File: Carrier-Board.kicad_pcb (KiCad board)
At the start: 4 copper layers, 92 x 96 mm, 50 parts, among them J1 CONN_3-6318491-6, J10 Conn_02x03_Odd_Even, J2 Conn_01x0, J4 SI-51009-F, J6 Conn_01x03_Male, J7 Conn_01x03_Male, J8 Conn_01x06_Male, J9 Conn_02x04_Odd_Even, SW1 SW_Push, SW2 SW_Push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

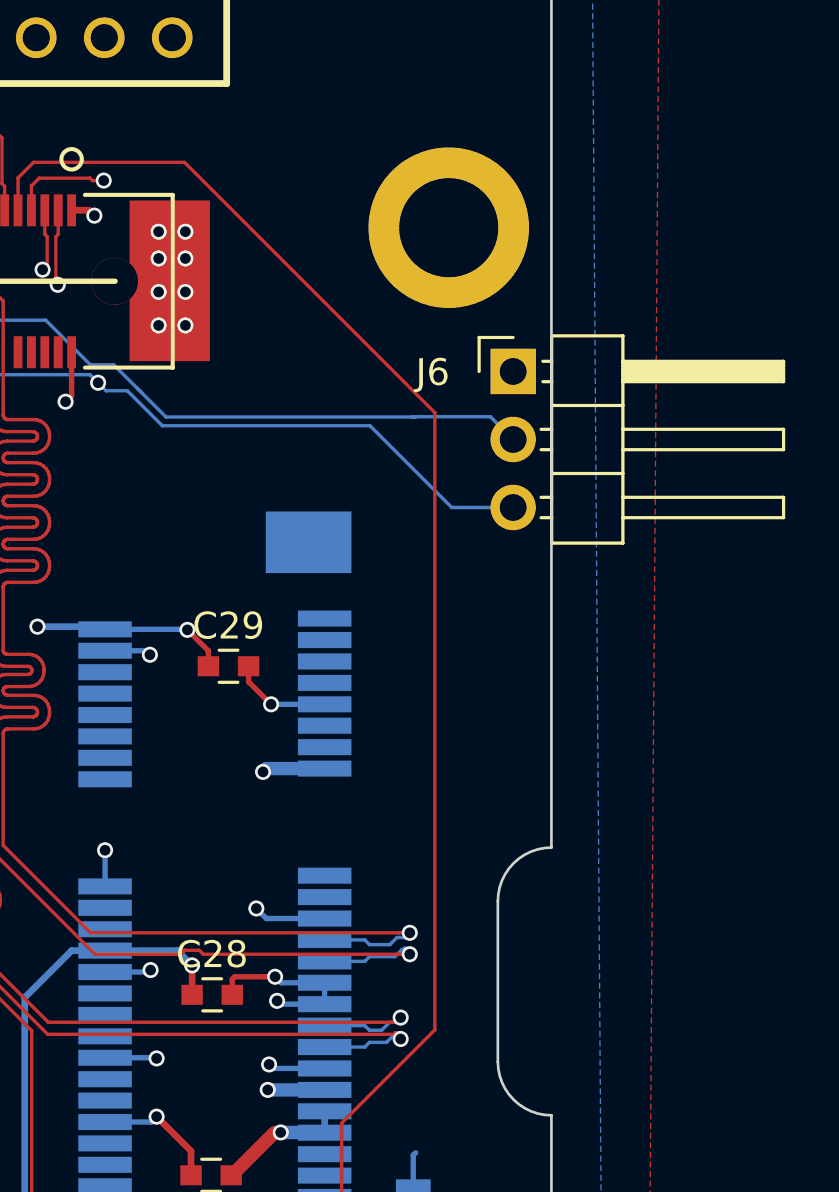
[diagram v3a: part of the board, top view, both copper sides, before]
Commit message: fixed a connector
connector too close to edge.
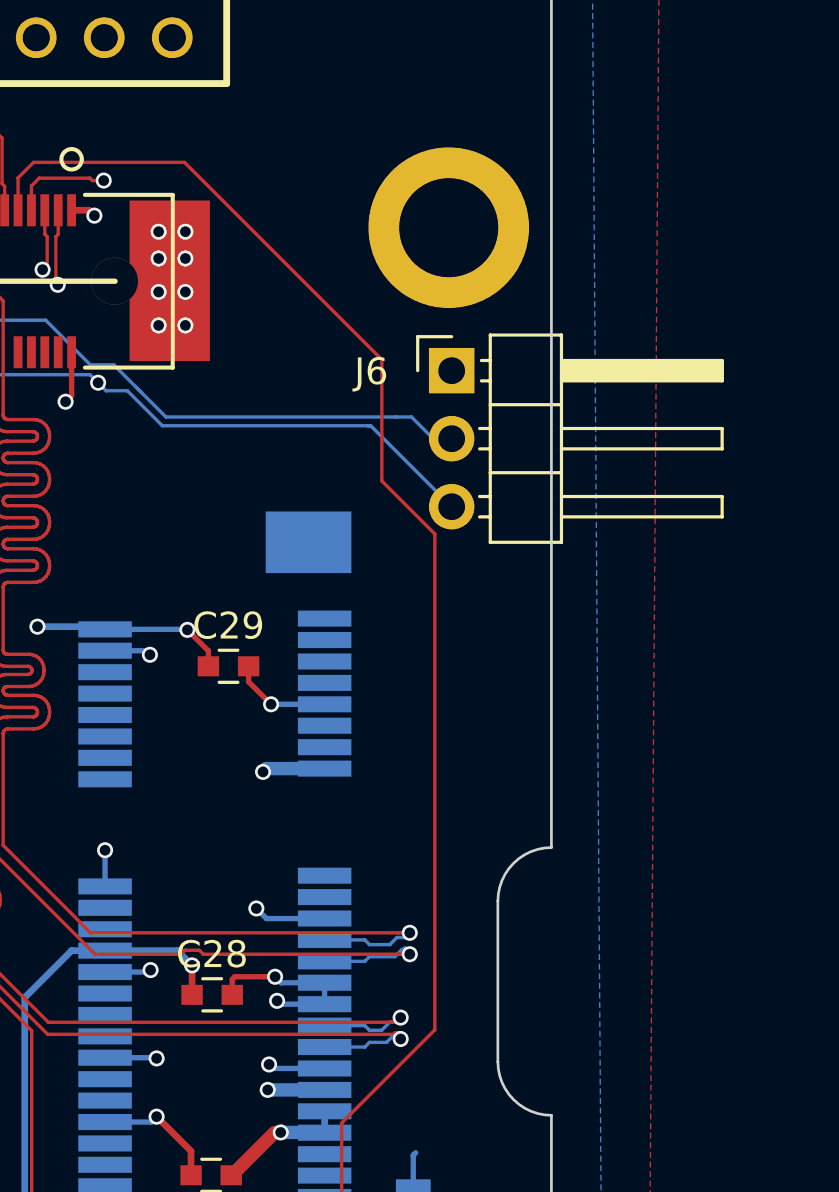
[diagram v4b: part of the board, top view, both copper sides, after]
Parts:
- moved J6 2.30 mm to (170.2, 49.2)
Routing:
- net I2C_DAT: track 37.4 -> 34.9 mm
- net I2C_CK: track 35.8 -> 33.6 mm
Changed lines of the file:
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@@
     (thickness 1.6)
     (drawings 7)
-    (tracks 3727)
+    (tracks 3729)
     (zones 0)
     (modules 50)
@@
   )
   (module Pin_Headers:Pin_Header_Angled_1x03_Pitch2.54mm (layer F.Cu)
-    (at 172.49 49.22)
+    (at 170.195 49.19)
     (descr "Through hole angled pin header, 1x03, 2.54mm pitch, 6mm pin length, single row")
     (tags "Through hole angled pin header THT 1x03 2.54mm single row")
@@
     (fp_line (start 10.55 6.85) (end 10.55 -1.8) (layer F.CrtYd) (width 0.05))
     (fp_line (start 10.55 -1.8) (end -1.8 -1.8) (layer F.CrtYd) (width 0.05))
-    (fp_text user %R (at 2.77 2.54 90) (layer F.Fab)
+    (fp_text user %R (at 2.67 2.49 90) (layer F.Fab)
       (effects (font (size 1 1) (thickness 0.15)))
     )
@@
     (at 161.35 57.75 270)
     (tags "mpci, pci, pci express")
-    (fp_text reference U9 (at -2.64 -7.675 540) (layer B.SilkS)
+    (fp_text reference U9 (at -5.01 4.095 540) (layer B.SilkS)
       (effects (font (thickness 0.15)) (justify mirror))
     )
@@
   (segment (start 124.695001 111.279999) (end 124.695001 111.265) (width 0.25) (layer F.Cu) (net 6))
   (segment (start 127.57 109.665) (end 127.57 111.465) (width 1) (layer F.Cu) (net 6))
+  (segment (start 167.075 51.247011) (end 167.147011 51.247011) (width 0.127) (layer B.Cu) (net 7))
+  (segment (start 159.389433 51.247011) (end 167.075 51.247011) (width 0.127) (layer B.Cu) (net 7))
+  (segment (start 167.075 51.247011) (end 167.172011 51.247011) (width 0.127) (layer B.Cu) (net 7))
+  (segment (start 167.172011 51.247011) (end 170.195 54.27) (width 0.127) (layer B.Cu) (net 7))
   (segment (start 145.981017 49.340001) (end 145.681018 49.64) (width 0.127) (layer B.Cu) (net 7))
   (segment (start 156.690001 49.340001) (end 145.981017 49.340001) (width 0.127) (layer B.Cu) (net 7))
@@
   (segment (start 158.082422 49.939999) (end 159.389433 51.247011) (width 0.127) (layer B.Cu) (net 7))
   (segment (start 157.289999 49.939999) (end 158.082422 49.939999) (width 0.127) (layer B.Cu) (net 7))
-  (segment (start 159.389433 51.247011) (end 167.147011 51.247011) (width 0.127) (layer B.Cu) (net 7))
-  (segment (start 167.147011 51.247011) (end 170.2 54.3) (width 0.127) (layer B.Cu) (net 7))
-  (segment (start 170.2 54.3) (end 172.49 54.3) (width 0.127) (layer B.Cu) (net 7))
   (segment (start 140.28 49.64) (end 140.27 49.65) (width 0.25) (layer B.Cu) (net 7))
   (segment (start 140.27 49.65) (end 140.000001 49.380001) (width 0.25) (layer F.Cu) (net 7))
@@
   (segment (start 156.99 49.8) (end 156.99 49.64) (width 0.25) (layer F.Cu) (net 7))
   (via (at 156.99 49.64) (size 0.6) (drill 0.4) (layers F.Cu B.Cu) (net 7))
+  (segment (start 168.105 50.920001) (end 159.524884 50.920001) (width 0.127) (layer B.Cu) (net 8))
+  (segment (start 169.505 51.73) (end 168.695001 50.920001) (width 0.127) (layer B.Cu) (net 8))
+  (segment (start 168.695001 50.920001) (end 168.105 50.920001) (width 0.127) (layer B.Cu) (net 8))
+  (segment (start 170.195 51.73) (end 169.505 51.73) (width 0.127) (layer B.Cu) (net 8))
   (segment (start 155.034556 47.305) (end 156.701485 48.971929) (width 0.127) (layer B.Cu) (net 8))
   (segment (start 140.183501 46.461499) (end 141.295481 46.461499) (width 0.127) (layer B.Cu) (net 8))
@@
   (segment (start 139.34 47.305) (end 140.183501 46.461499) (width 0.127) (layer B.Cu) (net 8))
   (segment (start 146.495481 46.686499) (end 151.095481 46.686499) (width 0.127) (layer B.Cu) (net 8))
-  (segment (start 168.850001 50.920001) (end 168.72 50.920001) (width 0.127) (layer B.Cu) (net 8))
-  (segment (start 168.72 50.920001) (end 159.524884 50.920001) (width 0.127) (layer B.Cu) (net 8))
-  (segment (start 172.49 51.76) (end 171.640001 50.910001) (width 0.127) (layer B.Cu) (net 8))
-  (segment (start 171.640001 50.910001) (end 168.73 50.910001) (width 0.127) (layer B.Cu) (net 8))
-  (segment (start 168.73 50.910001) (end 168.72 50.920001) (width 0.127) (layer B.Cu) (net 8))
   (segment (start 158.61 50.005117) (end 158.45 49.845117) (width 0.127) (layer B.Cu) (net 8))
   (segment (start 159.524884 50.920001) (end 158.45 49.845117) (width 0.127) (layer B.Cu) (net 8))
@@
   (segment (start 156.775736 42.09) (end 156.685736 42) (width 0.127) (layer F.Cu) (net 41))
   (via (at 157.2 42.09) (size 0.6) (drill 0.4) (layers F.Cu B.Cu) (net 41))
+  (segment (start 167.587298 48.78) (end 160.217298 41.41) (width 0.127) (layer F.Cu) (net 42))
+  (segment (start 169.565 73.81) (end 169.565 55.287982) (width 0.127) (layer F.Cu) (net 42))
+  (segment (start 169.565 55.287982) (end 167.587298 53.31028) (width 0.127) (layer F.Cu) (net 42))
+  (segment (start 167.587298 53.31028) (end 167.587298 48.78) (width 0.127) (layer F.Cu) (net 42))
   (segment (start 161.14 100.67) (end 162.306726 100.67) (width 0.127) (layer F.Cu) (net 42))
   (segment (start 154.000001 41.989999) (end 154.000001 43.2) (width 0.127) (layer F.Cu) (net 42))
@@
   (segment (start 162.92886 88.820433) (end 162.899712 88.759907) (width 0.127) (layer F.Cu) (net 42))
   (segment (start 162.970746 88.44869) (end 163.023269 88.406805) (width 0.127) (layer F.Cu) (net 42))
-  (segment (start 169.565 50.757702) (end 160.217298 41.41) (width 0.127) (layer F.Cu) (net 42))
   (segment (start 162.899712 88.561739) (end 162.92886 88.501213) (width 0.127) (layer F.Cu) (net 42))
   (segment (start 162.92886 88.501213) (end 162.970746 88.44869) (width 0.127) (layer F.Cu) (net 42))
@@
   (segment (start 166.085 86.68) (end 166.085 77.29) (width 0.127) (layer F.Cu) (net 42))
   (segment (start 163.149289 88.362709) (end 163.216467 88.36271) (width 0.127) (layer F.Cu) (net 42))
-  (segment (start 169.565 73.81) (end 169.565 50.757702) (width 0.127) (layer F.Cu) (net 42))
   (segment (start 163.216467 88.36271) (end 163.281962 88.377658) (width 0.127) (layer F.Cu) (net 42))
   (segment (start 163.39501 88.448691) (end 163.643529 88.69721) (width 0.127) (layer F.Cu) (net 42))

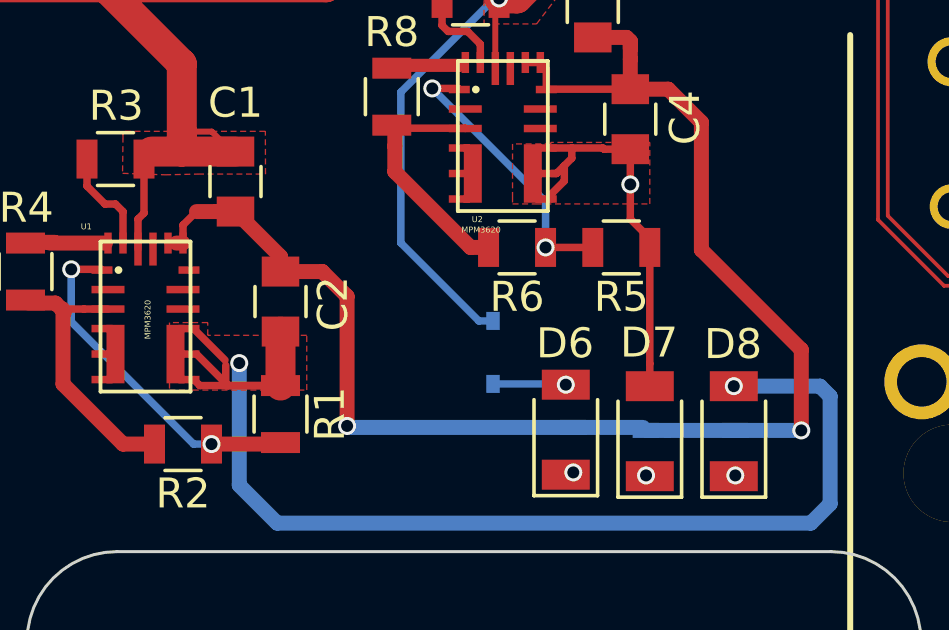
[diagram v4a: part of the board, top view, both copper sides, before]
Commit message: Fix some DRC errors
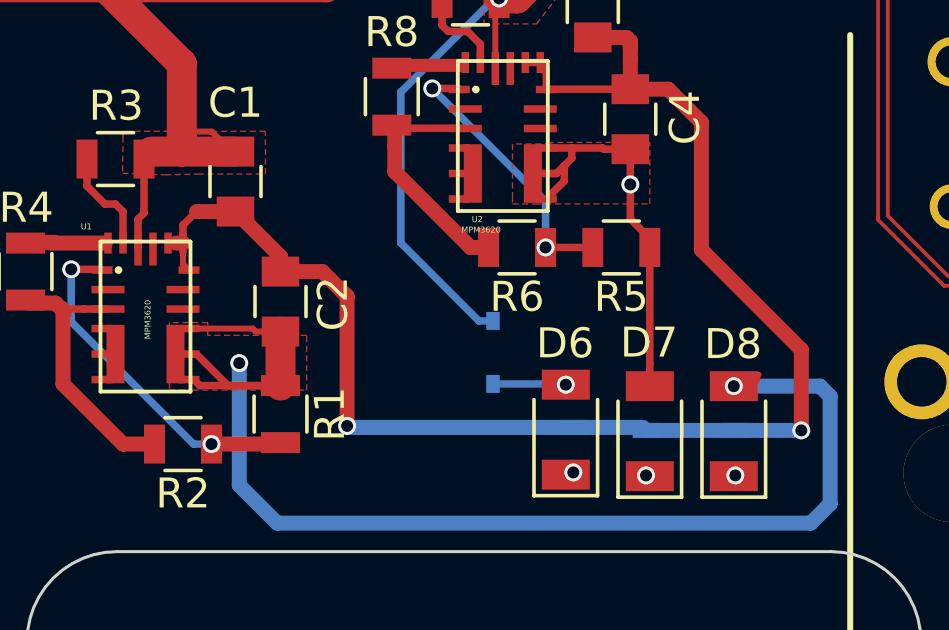
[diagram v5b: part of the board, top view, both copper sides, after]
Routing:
- net mCOM_5V_SBY: track 157.2 -> 159.8 mm
- net GBE0_CTREF(GND): track 190.3 -> 191.3 mm
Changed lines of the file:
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@@
     (thickness 1.6)
     (drawings 7)
-    (tracks 3729)
+    (tracks 3736)
     (zones 0)
     (modules 50)
@@
   (layers
     (0 F.Cu signal)
-    (1 In1.Cu power)
-    (2 In2.Cu power)
+    (1 In1.Cu power hide)
+    (2 In2.Cu power hide)
     (31 B.Cu signal)
     (32 B.Adhes user)
@@
   (via (at 139.755 114.46) (size 0.6) (drill 0.4) (layers F.Cu B.Cu) (net 4))
   (via (at 142.73 114.46) (size 0.6) (drill 0.4) (layers F.Cu B.Cu) (net 5))
+  (segment (start 142.68 111.485) (end 143.1246 111.485) (width 0.2) (layer F.Cu) (net 6))
+  (segment (start 143.1246 111.485) (end 143.507 111.1026) (width 0.2) (layer F.Cu) (net 6))
+  (segment (start 143.73 111.485) (end 142.68 111.485) (width 0.2) (layer B.Cu) (net 6))
+  (segment (start 142.68 111.485) (end 143.2516 111.485) (width 0.2) (layer F.Cu) (net 6))
+  (segment (start 143.2516 111.485) (end 143.4816 111.255) (width 0.2) (layer F.Cu) (net 6))
+  (segment (start 127.57 109.665) (end 126.745 109.665) (width 0.2) (layer F.Cu) (net 6))
+  (segment (start 126.745 109.665) (end 126.645 109.565) (width 0.2) (layer F.Cu) (net 6))
+  (segment (start 126.645 109.565) (end 124.670001 109.565) (width 0.2) (layer F.Cu) (net 6))
   (segment (start 91.474999 36.799999) (end 91.175 36.5) (width 1) (layer In2.Cu) (net 6))
   (segment (start 113.74 50.01) (end 113.74 47.220002) (width 1) (layer In2.Cu) (net 6))
@@
   (segment (start 113.72 50.03) (end 113.74 50.01) (width 0.5) (layer B.Cu) (net 6))
   (segment (start 90.15 36.475) (end 90.175 36.5) (width 0.25) (layer B.Cu) (net 6))
-  (segment (start 142.68 111.485) (end 143.73 111.485) (width 0.25) (layer B.Cu) (net 6))
   (via (at 142.68 111.485) (size 0.6) (drill 0.4) (layers F.Cu B.Cu) (net 6))
-  (segment (start 125.745001 111.465) (end 125.745001 110.790001) (width 0.25) (layer F.Cu) (net 6))
-  (segment (start 125.72 110.615) (end 124.67 109.565) (width 0.25) (layer F.Cu) (net 6))
   (segment (start 127.57 111.465) (end 125.745001 111.465) (width 0.25) (layer F.Cu) (net 6))
   (segment (start 125.82 111.465) (end 124.77 110.415) (width 0.25) (layer F.Cu) (net 6))
@@
   (segment (start 122.82 105.915) (end 122.82 106.915) (width 0.25) (layer F.Cu) (net 37))
   (segment (start 123.02 103.915) (end 123.02 105.715) (width 0.25) (layer F.Cu) (net 37))
+  (segment (start 124.32 106.715) (end 124.32 107.415) (width 0.2) (layer F.Cu) (net 38))
+  (segment (start 124.32 107.415) (end 124.52 107.615) (width 0.2) (layer F.Cu) (net 38))
   (segment (start 87.345 73.82) (end 87.345 76.03) (width 0.2) (layer B.Cu) (net 38))
   (segment (start 87.345 76.03) (end 87.275 76.1) (width 0.2) (layer B.Cu) (net 38))
@@
   )
   (zone (net 38) (net_name "GBE0_CTREF(GND)") (layer In2.Cu) (hatch edge 0.508)
+    (priority 3)
     (connect_pads yes (clearance 0.5))
     (min_thickness 0.254)
@@
   )
   (zone (net 38) (net_name "GBE0_CTREF(GND)") (layer In1.Cu) (hatch edge 0.508)
+    (priority 3)
     (connect_pads yes (clearance 0.5))
     (min_thickness 0.254)
@@
   )
   (zone (net 38) (net_name "GBE0_CTREF(GND)") (layer F.Cu) (hatch none 0.508)
+    (priority 3)
     (connect_pads yes (clearance 0.8))
     (min_thickness 0.254)
@@
   )
   (zone (net 38) (net_name "GBE0_CTREF(GND)") (layer B.Cu) (hatch edge 0.508)
+    (priority 3)
     (connect_pads yes (clearance 0.5))
     (min_thickness 0.254)

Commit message: sd
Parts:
- added REF**: MountingHole_3.2mm_M3, Mounting_Holes:MountingHole_3.2mm_M3, F.Cu at (91.1, 29.1)
- added REF**: MountingHole_3.2mm_M3, Mounting_Holes:MountingHole_3.2mm_M3, F.Cu at (87.3, 114.8)
- added REF**: MountingHole_3.2mm_M3, Mounting_Holes:MountingHole_3.2mm_M3, F.Cu at (167.3, 114.8)
- added REF**: MountingHole_3.2mm_M3, Mounting_Holes:MountingHole_3.2mm_M3, F.Cu at (164.8, 29.1)
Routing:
- net mCOM_5V_SBY: track 159.8 -> 160.5 mm
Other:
- board text added: "S/N: 0C137"
- board text removed: "S/N: 00000000"
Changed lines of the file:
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@@
 (kicad_pcb (version 4) (host pcbnew 4.0.7)
   (general
-    (links 180)
+    (links 0)
     (no_connects 2)
     (area 73.267618 18.99 188.200001 129.325001)
     (thickness 1.6)
     (drawings 7)
-    (tracks 3736)
+    (tracks 3740)
     (zones 0)
-    (modules 50)
+    (modules 54)
     (nets 335)
   )
@@
   (layers
     (0 F.Cu signal)
-    (1 In1.Cu power hide)
-    (2 In2.Cu power hide)
+    (1 In1.Cu power)
+    (2 In2.Cu power)
     (31 B.Cu signal)
     (32 B.Adhes user)
@@
     (add_net WAKE1n)
   )
+  (module Mounting_Holes:MountingHole_3.2mm_M3 (layer F.Cu)
+    (at 91.135 29.09)
+    (descr "Mounting Hole 3.2mm, no annular, M3")
+    (tags "mounting hole 3.2mm no annular m3")
+    (attr virtual)
+    (fp_text reference REF** (at 0 -4.2) (layer F.SilkS)
+      (effects (font (size 1 1) (thickness 0.15)))
+    )
+    (fp_text value MountingHole_3.2mm_M3 (at 0 4.2) (layer F.Fab)
+      (effects (font (size 1 1) (thickness 0.15)))
+    )
+    (fp_text user %R (at 0.3 0) (layer F.Fab)
+      (effects (font (size 1 1) (thickness 0.15)))
+    )
+    (fp_circle (center 0 0) (end 3.2 0) (layer Cmts.User) (width 0.15))
+    (fp_circle (center 0 0) (end 3.45 0) (layer F.CrtYd) (width 0.05))
+    (pad 1 np_thru_hole circle (at 0 0) (size 3.2 3.2) (drill 3.2) (layers *.Cu *.Mask))
+  )
+  (module Mounting_Holes:MountingHole_3.2mm_M3 (layer F.Cu)
+    (at 87.305 114.82)
+    (descr "Mounting Hole 3.2mm, no annular, M3")
+    (tags "mounting hole 3.2mm no annular m3")
+    (attr virtual)
+    (fp_text reference REF** (at 0 -4.2) (layer F.SilkS)
+      (effects (font (size 1 1) (thickness 0.15)))
+    )
+    (fp_text value MountingHole_3.2mm_M3 (at 0 4.2) (layer F.Fab)
+      (effects (font (size 1 1) (thickness 0.15)))
+    )
+    (fp_text user %R (at 0.3 0) (layer F.Fab)
+      (effects (font (size 1 1) (thickness 0.15)))
+    )
+    (fp_circle (center 0 0) (end 3.2 0) (layer Cmts.User) (width 0.15))
+    (fp_circle (center 0 0) (end 3.45 0) (layer F.CrtYd) (width 0.05))
+    (pad 1 np_thru_hole circle (at 0 0) (size 3.2 3.2) (drill 3.2) (layers *.Cu *.Mask))
+  )
+  (module Mounting_Holes:MountingHole_3.2mm_M3 (layer F.Cu)
+    (at 167.325 114.82)
+    (descr "Mounting Hole 3.2mm, no annular, M3")
+    (tags "mounting hole 3.2mm no annular m3")
+    (attr virtual)
+    (fp_text reference REF** (at 0 -4.2) (layer F.SilkS)
+      (effects (font (size 1 1) (thickness 0.15)))
+    )
+    (fp_text value MountingHole_3.2mm_M3 (at 0 4.2) (layer F.Fab)
+      (effects (font (size 1 1) (thickness 0.15)))
+    )
+    (fp_text user %R (at 0.3 0) (layer F.Fab)
+      (effects (font (size 1 1) (thickness 0.15)))
+    )
+    (fp_circle (center 0 0) (end 3.2 0) (layer Cmts.User) (width 0.15))
+    (fp_circle (center 0 0) (end 3.45 0) (layer F.CrtYd) (width 0.05))
+    (pad 1 np_thru_hole circle (at 0 0) (size 3.2 3.2) (drill 3.2) (layers *.Cu *.Mask))
+  )
   (module Pin_Headers:Pin_Header_Angled_2x04_Pitch2.54mm (layer F.Cu)
     (at 87.775 96.68 180)
@@
     (pad E3 thru_hole circle (at 0 0) (size 6 6) (drill 3.7) (layers *.Cu *.Mask))
   )
+  (module Mounting_Holes:MountingHole_3.2mm_M3 (layer F.Cu)
+    (at 164.835 29.11)
+    (descr "Mounting Hole 3.2mm, no annular, M3")
+    (tags "mounting hole 3.2mm no annular m3")
+    (attr virtual)
+    (fp_text reference REF** (at 0 -4.2) (layer F.SilkS)
+      (effects (font (size 1 1) (thickness 0.15)))
+    )
+    (fp_text value MountingHole_3.2mm_M3 (at 0 4.2) (layer F.Fab)
+      (effects (font (size 1 1) (thickness 0.15)))
+    )
+    (fp_text user %R (at 0.3 0) (layer F.Fab)
+      (effects (font (size 1 1) (thickness 0.15)))
+    )
+    (fp_circle (center 0 0) (end 3.2 0) (layer Cmts.User) (width 0.15))
+    (fp_circle (center 0 0) (end 3.45 0) (layer F.CrtYd) (width 0.05))
+    (pad 1 np_thru_hole circle (at 0 0) (size 3.2 3.2) (drill 3.2) (layers *.Cu *.Mask))
+  )
   (gr_line (start 99.925 45.85) (end 157.625 45.85) (layer F.SilkS) (width 0.2))
-  (gr_text "S/N: 00000000" (at 113.25 107) (layer B.SilkS)
+  (gr_text "S/N: 0C137" (at 113.25 107) (layer B.SilkS)
     (effects (font (size 0.7 0.7) (thickness 0.175)) (justify mirror))
   )
@@
   (via (at 139.755 114.46) (size 0.6) (drill 0.4) (layers F.Cu B.Cu) (net 4))
   (via (at 142.73 114.46) (size 0.6) (drill 0.4) (layers F.Cu B.Cu) (net 5))
+  (segment (start 89.195 31.63) (end 89.205 31.63) (width 0.2) (layer B.Cu) (net 6))
+  (segment (start 89.205 31.63) (end 90.15 32.575) (width 0.2) (layer B.Cu) (net 6))
+  (segment (start 90.15 32.575) (end 90.15 32.775) (width 0.2) (layer B.Cu) (net 6))
+  (segment (start 85.835 28.27) (end 89.195 31.63) (width 0.2) (layer B.Cu) (net 6))
+  (segment (start 85.835 28.21) (end 85.835 28.27) (width 0.2) (layer B.Cu) (net 6))
+  (segment (start 85.855 28.19) (end 85.835 28.21) (width 0.2) (layer B.Cu) (net 6))
+  (segment (start 85.855 27.095) (end 85.855 28.19) (width 0.2) (layer B.Cu) (net 6))
+  (segment (start 86.825 26.575) (end 86.375 26.575) (width 0.2) (layer B.Cu) (net 6))
+  (segment (start 86.375 26.575) (end 85.855 27.095) (width 0.2) (layer B.Cu) (net 6))
   (segment (start 142.68 111.485) (end 143.1246 111.485) (width 0.2) (layer F.Cu) (net 6))
   (segment (start 143.1246 111.485) (end 143.507 111.1026) (width 0.2) (layer F.Cu) (net 6))
@@
   (segment (start 126.195 110.715) (end 121.695999 106.215999) (width 1) (layer In2.Cu) (net 6))
   (segment (start 114.039999 50.309999) (end 113.74 50.01) (width 1) (layer In2.Cu) (net 6))
-  (segment (start 86.825 26.575) (end 86.825 28.8) (width 0.5) (layer B.Cu) (net 6))
-  (segment (start 86.825 28.8) (end 87.625002 28.8) (width 0.5) (layer B.Cu) (net 6))
-  (segment (start 87.625002 28.8) (end 90.15 31.324998) (width 0.5) (layer B.Cu) (net 6))
-  (segment (start 90.15 31.324998) (end 90.15 31.825) (width 0.5) (layer B.Cu) (net 6))
-  (segment (start 90.15 31.825) (end 90.15 32.775) (width 0.5) (layer B.Cu) (net 6))
   (segment (start 91.575 33.125) (end 91.575 36.1) (width 0.5) (layer B.Cu) (net 6))
   (segment (start 91.575 36.1) (end 91.175 36.5) (width 0.5) (layer B.Cu) (net 6))
